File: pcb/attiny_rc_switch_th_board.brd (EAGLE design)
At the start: 14.7 x 25.4 mm, 14 parts, among them U1 ATTINY85-20PU, U2 MOSFET_N-CH_VN3205N3-GTO-92_M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

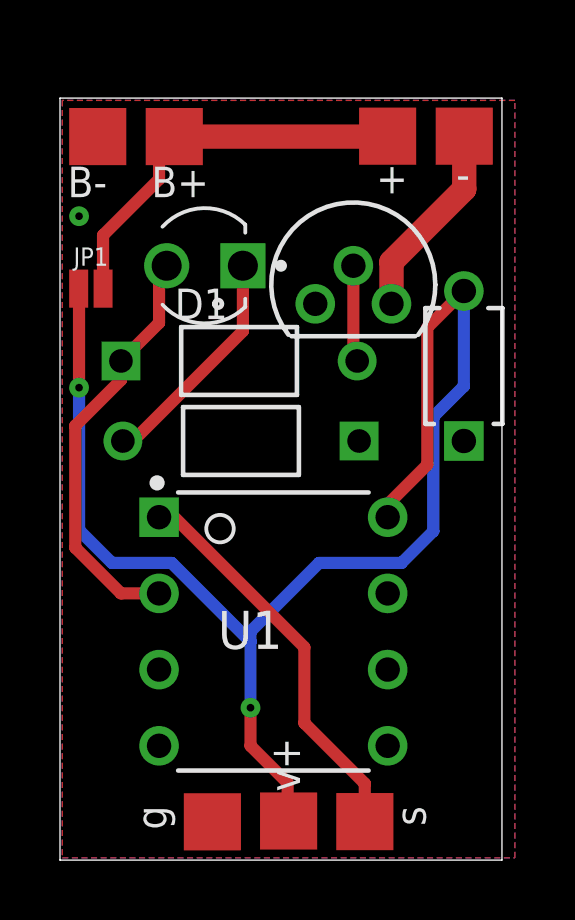
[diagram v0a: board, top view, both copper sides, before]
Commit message: fixed signal pin, changed pads
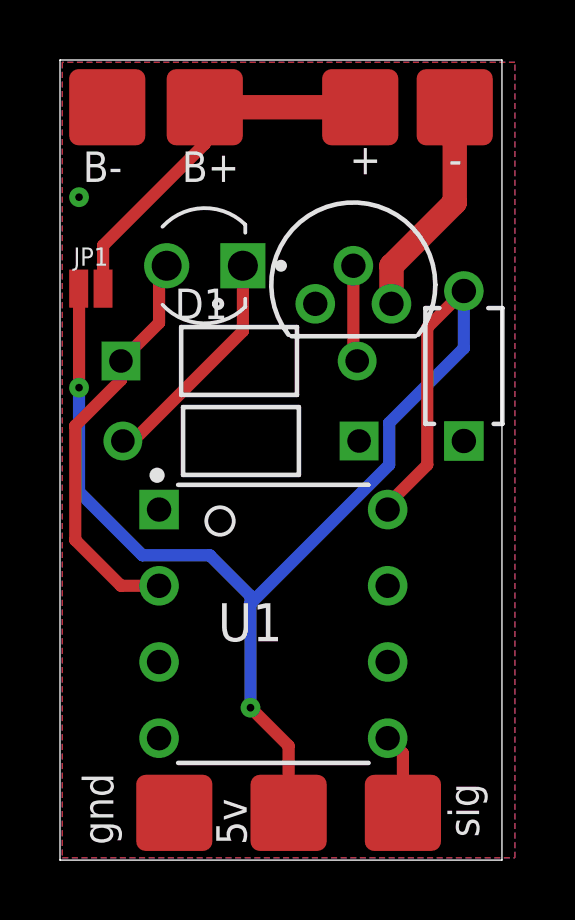
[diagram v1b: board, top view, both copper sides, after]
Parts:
- removed U$8: SMD_PAD, scotts-library:SMD_PAD
- added U$7: SMD_PAD_NO_STENCIL, scotts-library:SMD_PAD_NO_STENCIL
- U$1, U$2, U$3, U$4, U$5, U$6: value SMD_PAD -> SMD_PAD_NO_STENCIL; device scotts-library:SMD_PAD -> scotts-library:SMD_PAD_NO_STENCIL
- moved U$6 11.9 mm to (1.57, 25.1)
- moved U$3 9.40 mm to (13.2, 25.1)
- moved U$4 8.80 mm to (10.0, 25.1)
- moved U$5 6.17 mm to (4.83, 25.1)
- moved U$2 1.30 mm to (3.81, 1.57), turned to 0 degrees
- moved U$1 0.27 mm to (7.62, 1.57), turned to 0 degrees
- moved U1 0.25 mm to (7.11, 7.87)
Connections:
- removed net PB0: U1.5
- new net PB5: U1.1
- net GND: now also U$6.P$1; no longer U$4.P$1
- net OUT+: now also U$4.P$1; no longer U$3.P$1
- net OUT-: now also U$3.P$1; no longer U$6.P$1
- net SIG: now also U$7.P$1, U1.5; no longer U$8.P$1, U1.1
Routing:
- net SIG: track 13.3 -> 2.70 mm
- net 5V: track 46.7 -> 43.4 mm
- net OUT-: track 6.59 -> 7.43 mm
- net OUT+: track 13.2 -> 12.6 mm
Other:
- board size 14.7 x 25.4 mm -> 14.7 x 26.7 mm
- board text added: "5v"
- board text added: "gnd"
- board text added: "sig"
- board text removed: "g"
- board text removed: "s"
- board text removed: "v+"
